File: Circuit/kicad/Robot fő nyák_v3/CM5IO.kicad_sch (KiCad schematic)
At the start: 16 parts, among them J11 USB_C_Receptacle_USB2.0, J13 Molex 470531000, U49 EMC2301-1-ACZL-TR

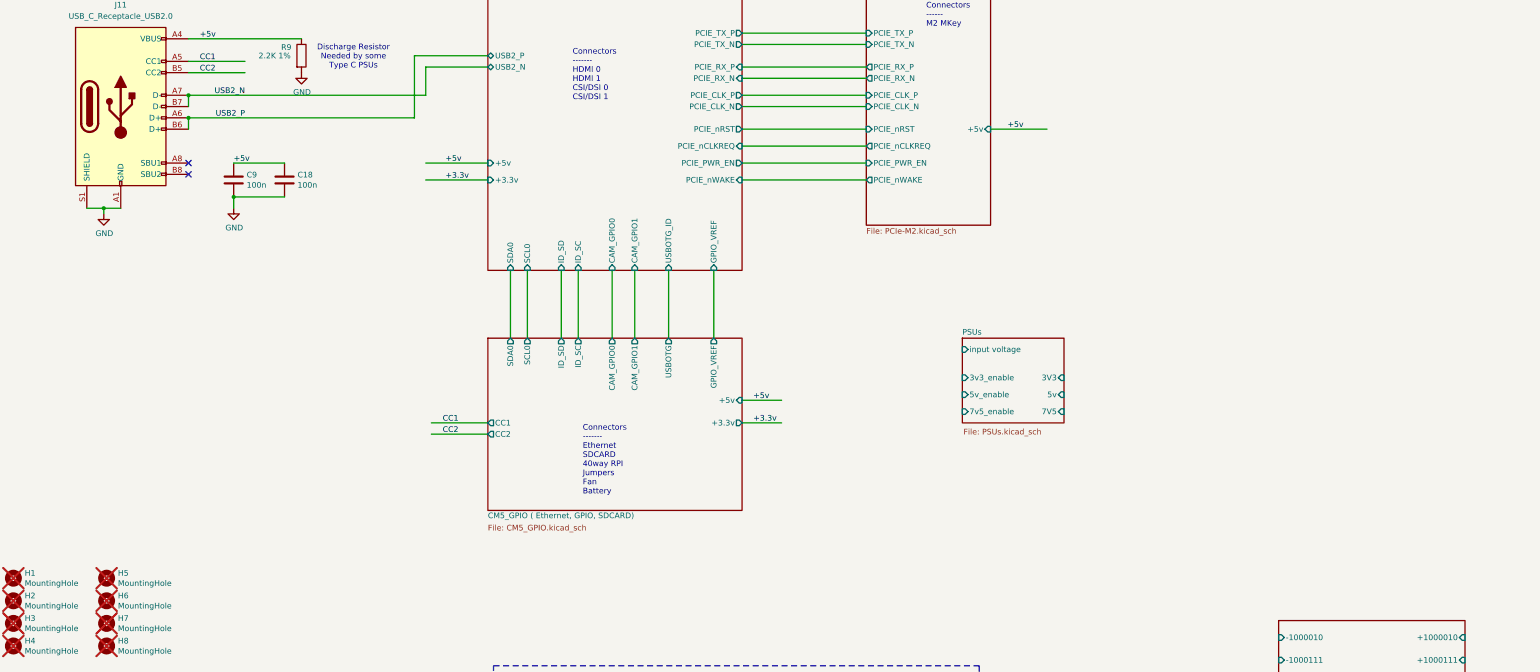
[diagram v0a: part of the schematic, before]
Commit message: kicad i2c schematic updated: gyto i2c bugfixes, +add new datasheets
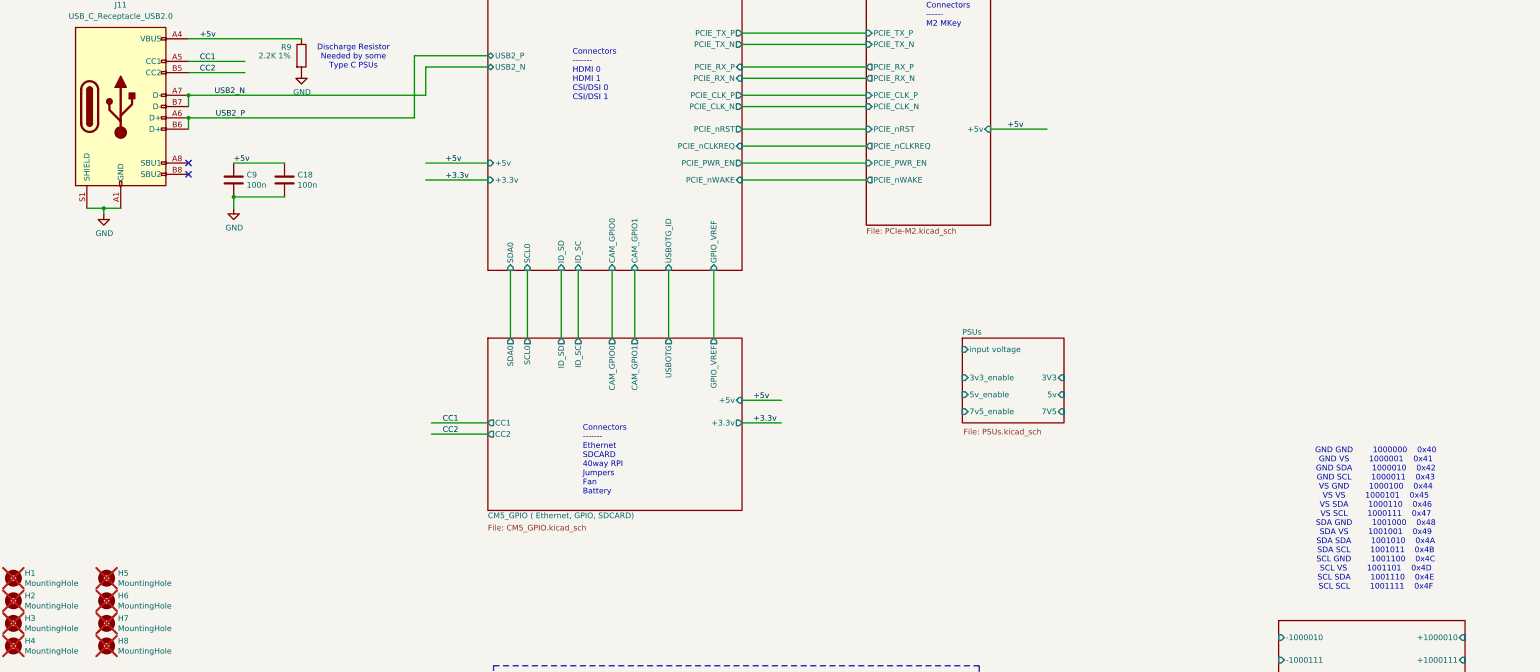
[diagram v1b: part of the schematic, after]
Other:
- note added: "GND GND 1000000 0x40 GND VS 1000001 0x41 GND SDA 1000010 0x42 GND SCL 1000011 0x43 VS GND 1000100 0x44 VS VS 1000101 0x45 VS SDA 1000110 0x46 VS SCL 1000111 0x47 SDA GND 1001000 0x48 SDA VS 1001001 0x49 SDA SDA 1001010 0x4A SDA SCL 1001011 0x4B SCL GND 1001100 0x4C SCL VS 1001101 0x4D SCL SDA 1001110 0x4E SCL SCL 1001111 0x4F"
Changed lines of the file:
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@@
 (kicad_sch
-	(version 20231120)
+	(version 20250114)
 	(generator "eeschema")
-	(generator_version "8.0")
+	(generator_version "9.0")
 	(paper "A0")
 	(title_block
@@
 		(comment 1 "www.raspberrypi.com")
 	)
+	(text "Connectors\n-------\nEthernet\nSDCARD\n40way RPI\nJumpers\nFan\nBattery"
+		(exclude_from_sim no)
+		(at 150.876 147.066 0)
+		(effects
+			(font
+				(size 1.27 1.27)
+			)
+			(justify left bottom)
+		)
+	)
+	(text "IIC address : 0101_111x"
+		(exclude_from_sim no)
+		(at 161.29 227.33 0)
+		(effects
+			(font
+				(size 1.27 1.27)
+			)
+			(justify left bottom)
+		)
+	)
+	(text "Connectors\n------\nM2 MKey"
+		(exclude_from_sim no)
+		(at 228.092 41.91 0)
+		(effects
+			(font
+				(size 1.27 1.27)
+			)
+			(justify left bottom)
+		)
+	)
+	(text "Discharge Resistor\nNeeded by some\nType C PSUs"
+		(exclude_from_sim no)
+		(at 99.314 48.514 0)
+		(effects
+			(font
+				(size 1.27 1.27)
+			)
+		)
+	)
+	(text "TypeC Power connector"
+		(exclude_from_sim no)
+		(at 36.068 33.528 0)
+		(effects
+			(font
+				(size 1.27 1.27)
+			)
+			(justify left bottom)
+		)
+	)
+	(text "GND GND		1000000	0x40\nGND VS		1000001	0x41\nGND SDA		1000010	0x42\nGND SCL		1000011	0x43\nVS GND		1000100	0x44\nVS VS		1000101	0x45\nVS SDA		1000110	0x46\nVS SCL		1000111	0x47\nSDA GND		1001000	0x48\nSDA VS		1001001	0x49\nSDA SDA		1001010	0x4A\nSDA SCL		1001011	0x4B\nSCL GND		1001100	0x4C\nSCL VS		1001101	0x4D\nSCL SDA		1001110	0x4E\nSCL SCL		1001111	0x4F"
+		(exclude_from_sim no)
+		(at 329.184 152.4 0)
+		(effects
+			(font
+				(size 1.27 1.27)
+			)
+		)
+	)
+	(text "Connectors\n-------\nHDMI 0\nHDMI 1\nCSI/DSI 0\nCSI/DSI 1"
+		(exclude_from_sim no)
+		(at 148.59 58.42 0)
+		(effects
+			(font
+				(size 1.27 1.27)
+			)
+			(justify left bottom)
+		)
+	)
+	(text "FAN controler"
+		(exclude_from_sim no)
+		(at 142.24 190.5 0)
+		(effects
+			(font
+				(size 2.0066 2.0066)
+			)
+			(justify left bottom)
+		)
+	)
+	(text "Also SMBUS alert IIC address : 0001_100x"
+		(exclude_from_sim no)
+		(at 161.3154 231.4194 0)
+		(effects
+			(font
+				(size 1.27 1.27)
+			)
+			(justify left bottom)
+		)
+	)
+	(text "FAN connector\n"
+		(exclude_from_sim no)
+		(at 217.17 209.55 0)
+		(effects
+			(font
+				(size 1.27 1.27)
+			)
+			(justify left bottom)
+		)
+	)
 	(junction
 		(at 184.15 218.44)
@@
 		)
 	)
-	(text "Connectors\n-------\nEthernet\nSDCARD\n40way RPI\nJumpers\nFan\nBattery"
-		(exclude_from_sim no)
-		(at 150.876 147.066 0)
-		(effects
-			(font
-				(size 1.27 1.27)
-			)
-			(justify left bottom)
-		)
-	)
-	(text "IIC address : 0101_111x"
-		(exclude_from_sim no)
-		(at 161.29 227.33 0)
-		(effects
-			(font
-				(size 1.27 1.27)
-			)
-			(justify left bottom)
-		)
-	)
-	(text "Connectors\n------\nM2 MKey"
-		(exclude_from_sim no)
-		(at 228.092 41.91 0)
-		(effects
-			(font
-				(size 1.27 1.27)
-			)
-			(justify left bottom)
-		)
-	)
-	(text "Discharge Resistor\nNeeded by some\nType C PSUs"
-		(exclude_from_sim no)
-		(at 99.314 48.514 0)
-		(effects
-			(font
-				(size 1.27 1.27)
-			)
-		)
-	)
-	(text "TypeC Power connector"
-		(exclude_from_sim no)
-		(at 36.068 33.528 0)
-		(effects
-			(font
-				(size 1.27 1.27)
-			)
-			(justify left bottom)
-		)
-	)
-	(text "Connectors\n-------\nHDMI 0\nHDMI 1\nCSI/DSI 0\nCSI/DSI 1"
-		(exclude_from_sim no)
-		(at 148.59 58.42 0)
-		(effects
-			(font
-				(size 1.27 1.27)
-			)
-			(justify left bottom)
-		)
-	)
-	(text "FAN controler"
-		(exclude_from_sim no)
-		(at 142.24 190.5 0)
-		(effects
-			(font
-				(size 2.0066 2.0066)
-			)
-			(justify left bottom)
-		)
-	)
-	(text "Also SMBUS alert IIC address : 0001_100x"
-		(exclude_from_sim no)
-		(at 161.3154 231.4194 0)
-		(effects
-			(font
-				(size 1.27 1.27)
-			)
-			(justify left bottom)
-		)
-	)
-	(text "FAN connector\n"
-		(exclude_from_sim no)
-		(at 217.17 209.55 0)
-		(effects
-			(font
-				(size 1.27 1.27)
-			)
-			(justify left bottom)
-		)
-	)
 	(label "+5v"
 		(at 72.39 72.39 0)
-		(fields_autoplaced yes)
 		(effects
 			(font
@@
 	(label "CC1"
 		(at 119.38 130.81 0)
-		(fields_autoplaced yes)
 		(effects
 			(font
@@
 	(label "CC2"
 		(at 119.38 133.35 0)
-		(fields_autoplaced yes)
 		(effects
 			(font
@@
 	(label "+5v"
 		(at 246.38 64.77 0)
-		(fields_autoplaced yes)
 		(effects
 			(font
@@
 	(label "+5v"
 		(at 189.23 125.73 0)
-		(fields_autoplaced yes)
 		(effects
 			(font
@@
 	(label "+5v"
 		(at 120.015 72.39 0)
-		(fields_autoplaced yes)
 		(effects
 			(font
@@
 	(label "USB2_P"
 		(at 74.93 62.23 180)
-		(fields_autoplaced yes)
 		(effects
 			(font
@@
 	(label "CC1"
 		(at 64.77 49.53 0)
-		(fields_autoplaced yes)
 		(effects
 			(font
@@
 	(label "USB2_N"
 		(at 74.93 57.15 180)
-		(fields_autoplaced yes)
 		(effects
 			(font
@@
 	(label "+3.3v"
 		(at 189.23 130.81 0)
-		(fields_autoplaced yes)
 		(effects
 			(font
@@
 	(label "+3.3v"
 		(at 120.015 76.2 0)
-		(fields_autoplaced yes)
 		(effects
 			(font
@@
 	(label "CC2"
 		(at 64.77 52.07 0)
-		(fields_autoplaced yes)
 		(effects
 			(font
@@
 	(label "+5v"
 		(at 64.77 44.45 0)
-		(fields_autoplaced yes)
 		(effects
 			(font
@@
 	(label "+3.3v"
 		(at 144.78 203.2 0)
-		(fields_autoplaced yes)
 		(effects
 			(font
@@
 		(shape input)
 		(at 143.51 203.2 180)
-		(fields_autoplaced yes)
 		(effects
 			(font
@@
 		(shape input)
 		(at 156.21 213.36 180)
-		(fields_autoplaced yes)
 		(effects
 			(font
@@
 		(shape input)
 		(at 156.21 215.9 180)
-		(fields_autoplaced yes)
 		(effects
 			(font
@@
 		(shape input)
 		(at 199.39 196.85 180)
-		(fields_autoplaced yes)
 		(effects
 			(font
@@
 		(at 129.54 111.76)
 		(size 57.15 38.735)
+		(exclude_from_sim no)
+		(in_bom yes)
+		(on_board yes)
+		(dnp no)
 		(stroke
 			(width 0.1524)
@@
 		(at 129.54 34.29)
 		(size 57.15 62.23)
+		(exclude_from_sim no)
+		(in_bom yes)
+		(on_board yes)
+		(dnp no)
 		(stroke
 			(width 0.1524)
@@
 		(at 214.63 34.29)
 		(size 27.94 52.07)
+		(exclude_from_sim no)
+		(in_bom yes)
+		(on_board yes)
+		(dnp no)
 		(fields_autoplaced yes)
 		(stroke
@@
 		(at 236.22 111.76)
 		(size 22.86 19.05)
+		(exclude_from_sim no)
+		(in_bom yes)
+		(on_board yes)
+		(dnp no)
 		(stroke
 			(width 0.1524)
@@
 		(at 307.34 175.26)
 		(size 41.91 82.55)
+		(exclude_from_sim no)
+		(in_bom yes)
+		(on_board yes)
+		(dnp no)
 		(stroke
 			(width 0.1524)
@@
 		(at 114.3 254)
 		(size 38.1 22.86)
+		(exclude_from_sim no)
+		(in_bom yes)
+		(on_board yes)
+		(dnp no)
 		(fields_autoplaced yes)
 		(stroke
@@
 		(at 38.1 252.73)
 		(size 55.88 71.12)
+		(exclude_from_sim no)
+		(in_bom yes)
+		(on_board yes)
+		(dnp no)
 		(stroke
 			(width 0.1524)
@@
 		)
 	)
+	(embedded_fonts no)
 )

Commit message: refactor(kicad): Simplify PCB by removing redundant fan controller
This commit refines the main KiCad PCB design by removing the external PWM fan controller circuit. This simplification is possible because the Raspberry Pi CM5 provides its own built-in fan control. Associated mounting points and components were also removed, cleaning up the board layout.
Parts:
- removed C18, C9: 100n, Capacitor_SMD:C_0402_1005Metric, symbol Device:C
- removed C54: 100n, Capacitor_SMD:C_0805_2012Metric, symbol Device:C
- removed J11: USB_C_Receptacle_USB2.0, Connector_USB:USB_C_Receptacle_GCT_USB4105-xx-A_16P_TopMnt_Horizontal, symbol Connector:USB_C_Receptacle_USB2.0_16P
- removed J13: Molex 470531000, Connector:FanPinHeader_1x04_P2.54mm_Vertical, symbol Connector_Generic:Conn_01x04
- removed R80: 36K 1%, Resistor_SMD:R_0805_2012Metric_Pad1.20x1.40mm_HandSolder, symbol Device:R
- removed R9: 2.2K 1%, Resistor_SMD:R_0402_1005Metric, symbol Device:R
- removed U49: EMC2301-1-ACZL-TR, Package_SO:MSOP-8_3x3mm_P0.65mm, symbol CM4IO:EMC2301
- added SW3: SW_DIP_x05, symbol Switch:SW_DIP_x05
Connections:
- net PSUs/3v3_enable: now also SW3.10
- net PSUs/5v_enable: now also SW3.9
- net PSUs/7v5_enable: now also SW3.8
- net PSUs/input voltage: now also SW3.1, SW3.2, SW3.3, SW3.4, SW3.5
- new net PSUs/12v_v1_enable: SW3.7
- new net PSUs/12v_v2_enable: SW3.6
- no-connect marks 4 -> 0
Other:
- sheet CM5_GPIO ( Ethernet, GPIO, SDCARD) ports: added none; removed USBOTG
- sheet PSUs ports: added 12V_v1, 12V_v2, 12v_v1_enable, 12v_v2_enable; removed none
- note removed: "Also SMBUS alert IIC address : 0001_100x"
- note removed: "Discharge Resistor Needed by some Type C PSUs"
- note removed: "FAN connector"
- note removed: "FAN controler"
- note removed: "IIC address : 0101_111x"
- note removed: "TypeC Power connector"
- moved on the sheet: H1, H2, H3, H4, H5, H6, H7, H8

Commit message: KICAD V3.01 Cleaned sheets + update + szekér modell add
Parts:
- removed H1, H2, H3, H4, H5, H6, H7, H8: MountingHole, CM5IO:MountingHole_2.7mm_M2.5_DIN965, symbol Mechanical:MountingHole
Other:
- company: Copyright © 2024 Raspberry Pi Ltd. -> (none)
- title: Compute Module 5 IO Board - Top Level -> (none)
- moved on the sheet: SW3

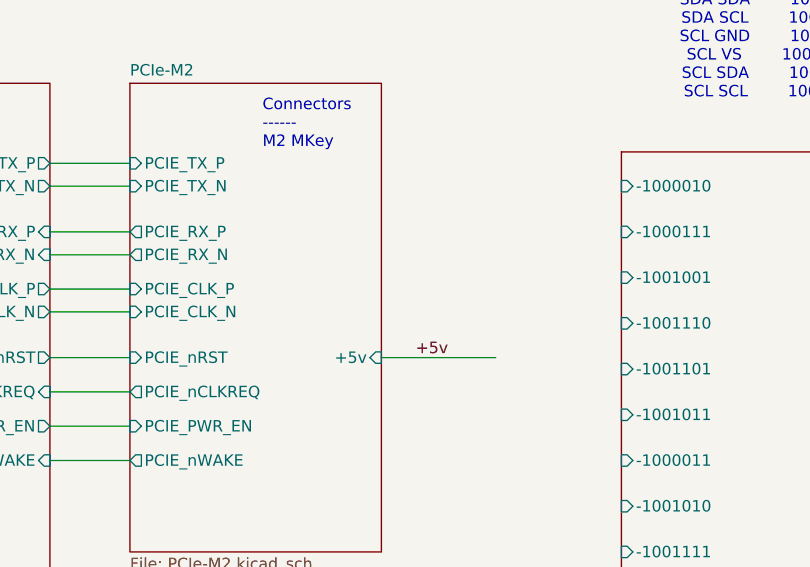
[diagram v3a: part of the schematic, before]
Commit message: M.2 power rail fixed
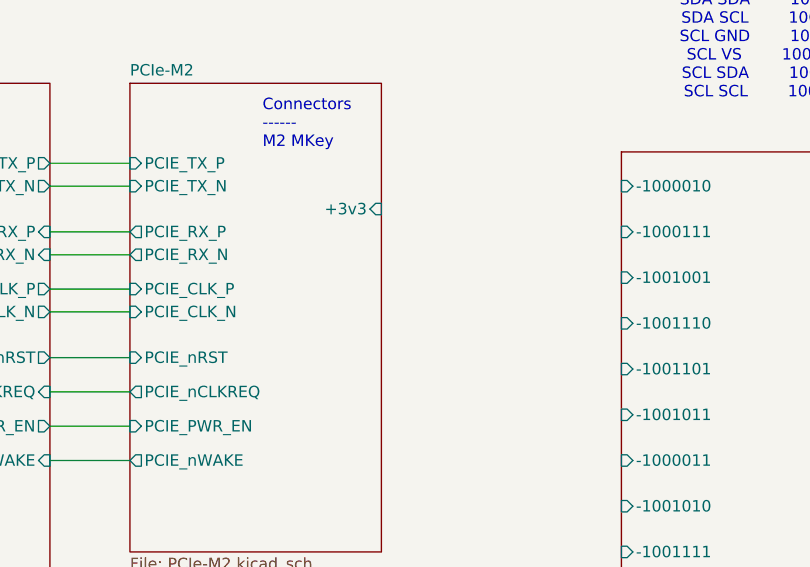
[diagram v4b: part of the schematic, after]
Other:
- sheet PCIe-M2 ports: added +3v3; removed +5v
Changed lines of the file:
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@@
 	(wire
 		(pts
-			(xy 195.58 95.25) (xy 208.28 95.25)
+			(xy 85.09 34.29) (xy 105.41 34.29)
+		)
+		(stroke
+			(width 0)
+			(type default)
+		)
+	)
+	(wire
+		(pts
+			(xy 158.75 102.87) (xy 167.64 102.87)
+		)
+		(stroke
+			(width 0)
+			(type default)
+		)
+	)
+	(wire
+		(pts
+			(xy 158.75 90.17) (xy 167.64 90.17)
 		)
 		(stroke
@@
 	(wire
 		(pts
-			(xy 85.09 34.29) (xy 105.41 34.29)
+			(xy 85.09 27.94) (xy 105.41 27.94)
 		)
 		(stroke
@@
 	(wire
 		(pts
-			(xy 158.75 102.87) (xy 167.64 102.87)
+			(xy 118.11 127) (xy 118.11 142.24)
+		)
+		(stroke
+			(width 0)
+			(type solid)
+		)
+	)
+	(wire
+		(pts
+			(xy 158.75 156.21) (xy 167.64 156.21)
 		)
 		(stroke
@@
 	(wire
 		(pts
-			(xy 158.75 90.17) (xy 167.64 90.17)
+			(xy 87.63 102.87) (xy 101.6 102.87)
 		)
 		(stroke
@@
 	(wire
 		(pts
-			(xy 85.09 27.94) (xy 105.41 27.94)
+			(xy 158.75 76.2) (xy 167.64 76.2)
+		)
+		(stroke
+			(width 0)
+			(type solid)
+		)
+	)
+	(wire
+		(pts
+			(xy 26.67 154.94) (xy 26.67 157.48)
 		)
 		(stroke
@@
 	(wire
 		(pts
-			(xy 118.11 127) (xy 118.11 142.24)
-		)
-		(stroke
-			(width 0)
-			(type solid)
-		)
-	)
-	(wire
-		(pts
-			(xy 158.75 156.21) (xy 167.64 156.21)
+			(xy 158.75 106.68) (xy 167.64 106.68)
 		)
 		(stroke
@@
 	(wire
 		(pts
-			(xy 87.63 102.87) (xy 101.6 102.87)
-		)
-		(stroke
-			(width 0)
-			(type solid)
-		)
-	)
-	(wire
-		(pts
-			(xy 158.75 76.2) (xy 167.64 76.2)
-		)
-		(stroke
-			(width 0)
-			(type solid)
-		)
-	)
-	(wire
-		(pts
-			(xy 26.67 154.94) (xy 26.67 157.48)
+			(xy 41.91 149.86) (xy 41.91 147.32)
 		)
 		(stroke
 			(width 0)
 			(type default)
-		)
-	)
-	(wire
-		(pts
-			(xy 158.75 106.68) (xy 167.64 106.68)
-		)
-		(stroke
-			(width 0)
-			(type default)
-		)
-	)
-	(wire
-		(pts
-			(xy 41.91 149.86) (xy 41.91 147.32)
-		)
-		(stroke
-			(width 0)
-			(type default)
-		)
-	)
-	(label "+5v"
-		(at 199.39 95.25 0)
-		(effects
-			(font
-				(size 1.27 1.27)
-			)
-			(justify left bottom)
 		)
 	)
@@
 			)
 		)
-		(pin "+5v" input
-			(at 195.58 95.25 0)
-			(effects
-				(font
-					(size 1.27 1.27)
-				)
-				(justify right)
-			)
-		)
 		(pin "PCIE_PWR_EN" input
 			(at 167.64 102.87 180)
@@
 			)
 		)
+		(pin "+3v3" input
+			(at 195.58 78.74 0)
+			(effects
+				(font
+					(size 1.27 1.27)
+				)
+				(justify right)
+			)
+		)
